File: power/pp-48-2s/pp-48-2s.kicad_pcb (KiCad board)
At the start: 4 copper layers, 150 x 80 mm, 178 parts, among them J1 BUS 40-60V, J101 NODE 1, J2 CTRL IN, J201 NODE 2, J3 CTRL OUT, J4 12V AUX OUT, J5 SWD, Q1 2N7002, Q101 BSC070N10NS5, Q102 2N7002, Q103 2N7002, Q104 2N7002, Q201 BSC070N10NS5, Q202 2N7002, Q203 2N7002, Q204 2N7002, U1 LM5164DDA, U101 LM5069MM-2, U102 INA238AIDGSR, U103 74LVC1G74, U104 TLP176AM, U105 TLP176AM, U106 TLP291, U2 LM5164DDA, U201 LM5069MM-2, U202 INA238AIDGSR, U203 74LVC1G74, U204 TLP176AM, U205 TLP176AM, U206 TLP291, U3 STM32G0B1CBT6, U4 ISO1640BD, U5 ISO7721D, U6 MCP23017-E/SO, X101 PM-19V-200W, X102 J2 AUX, X201 PM-19V-200W, X202 J2 AUX, Y1 8MHz

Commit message: power: PP-48-2S WIP checkpoint: placed, power copper, gndpour, KRT routed
tools/place.py (sockets, node connectors, bus terminal, MCU corner),
tools/power.py (VBUS trunk/artery/bar on B.Cu, slot SENSE/OUT/NODE,
GND stubs for fine-pitch pads, GND zones into the kept group),
tools/syncfields.py; gensch.py fills LCSC numbers (116 of 174).
Outline 150 x 95 mm, clearance 0.15 mm, KRT with --ordering mps
--no-stub-layer-swap. DRC: 4 unconnected (+3V3 C203, /FB2 C13,
/S1_ID U3, /S1_LQ U103), 2 clearance (S1_OUT/S1_PGD 0.149 mm),
3 starved thermals, silk untouched. Netlist pp-48-2s.xml matches
the schematic.
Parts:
- moved C25 371.0 mm to (239.0, 135.5)
- moved U3 368.3 mm to (229.0, 113.0)
- moved U4 364.7 mm to (239.0, 113.0), turned to 90 degrees
- moved R20 362.9 mm to (242.5, 150.0)
- moved C26 360.3 mm to (242.0, 135.5)
- moved JP2 359.8 mm to (237.5, 153.0)
- moved R28 358.4 mm to (236.0, 140.5)
- moved J2 352.4 mm to (245.8, 118.5), turned to 90 degrees
- moved R21 348.8 mm to (242.5, 153.0)
- moved U5 348.2 mm to (239.0, 122.0), turned to 90 degrees
- moved R29 347.5 mm to (239.0, 140.5)
- moved JP3 346.3 mm to (237.5, 156.0)
- moved C205 343.7 mm to (210.0, 166.0)
- moved C27 341.8 mm to (236.0, 138.0)
- moved U2 341.7 mm to (183.0, 108.0)
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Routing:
- net GND: track 0.00 -> 947.4 mm, vias 0 -> 261
- net +3V3: track 0.00 -> 475.4 mm, vias 0 -> 55
- net /VBUS: track 0.00 -> 310.3 mm, vias 0 -> 21
- net /SCL2: track 0.00 -> 219.7 mm, vias 0 -> 19
- net /SDA2: track 0.00 -> 205.8 mm, vias 0 -> 21
- net /S1_OFF: track 0.00 -> 177.5 mm, vias 0 -> 6
- net /S1_LED: track 0.00 -> 168.9 mm, vias 0 -> 10
- net /S2_NODE: track 0.00 -> 159.9 mm
- net /S1_LCLR: track 0.00 -> 159.4 mm, vias 0 -> 15
- net /S1_LQ: track 0.00 -> 140.1 mm, vias 0 -> 10
- net /S1_PGD: track 0.00 -> 139.4 mm, vias 0 -> 8
- net /S1_NODE: track 0.00 -> 137.8 mm
- net /VBUS_SNS: track 0.00 -> 130.2 mm, vias 0 -> 2
- net /S1_TEMP: track 0.00 -> 125.8 mm, vias 0 -> 8
- net /S1_PG: track 0.00 -> 119.0 mm, vias 0 -> 6
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- added copper zone on B.Cu, net GND
- added copper zone on F.Cu, net GND
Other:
- board size 150 x 80 mm -> 150 x 95 mm

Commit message: power: PP-48-2S opens closed by hand, DRC 0 unconnected / 0 clearance
tools/handroute/10-60: +3V3 C203.1, /FB2 C13.1 (+12V tap via moved
right of C13.2), /S1_LQ U103.5 (via between the pad rows, PWR west),
S1_PGD diagonal off the S1_OUT corner, /S1_ID to the MCU (via under the
LQFP body, PWR lane at y 133.3), +3V3 pad stubs restored after prune.
Dangling KRT leftovers pruned, GND refilled. Left: 4 starved_thermal
warnings, silk. Flow comment in pcbkit.toml, handoff updated.
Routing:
- net /S1_ID: track 54.5 -> 140.7 mm, vias 5 -> 6
- net GND: track 947.4 -> 907.5 mm
- net /S1_LQ: track 140.1 -> 147.4 mm
- net +3V3: track 475.4 -> 482.1 mm, vias 55 -> 56
- net /FB2: track 25.0 -> 28.1 mm
- net +12V: track 78.7 -> 79.8 mm

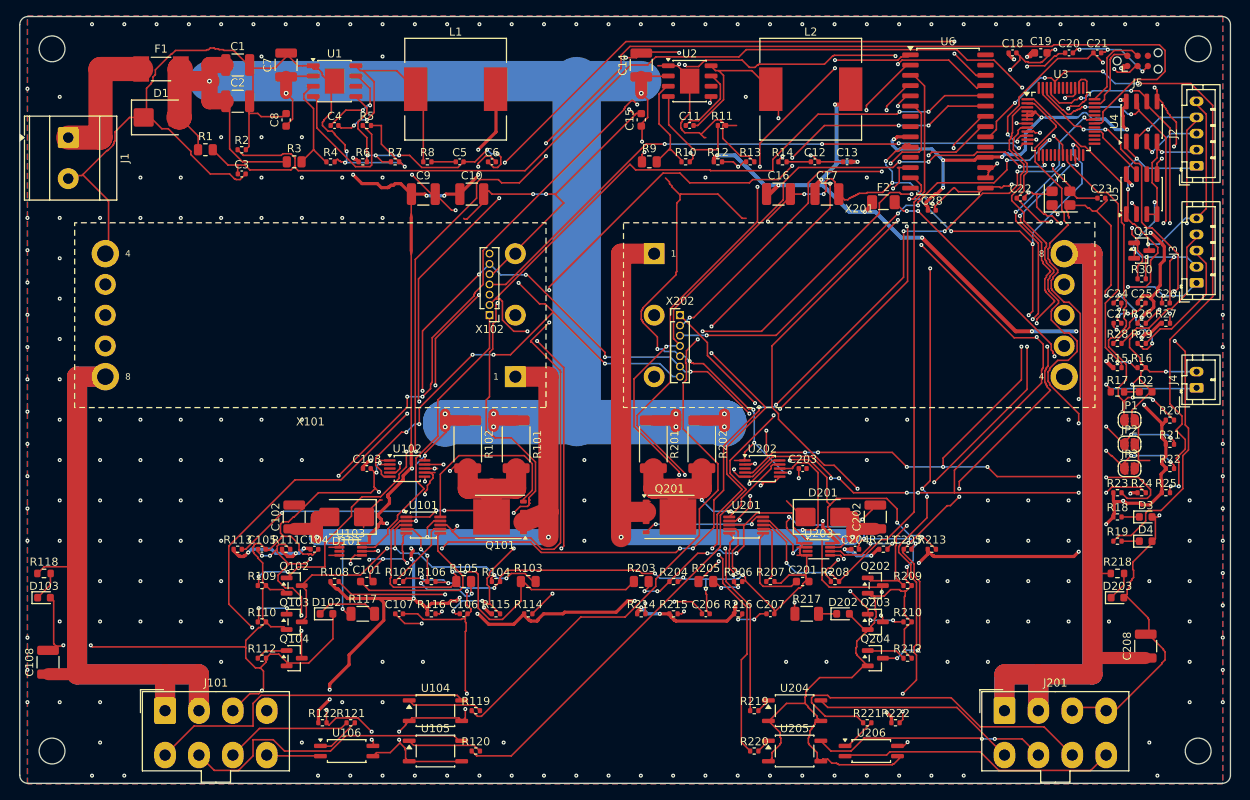
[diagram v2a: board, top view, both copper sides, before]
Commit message: power: PP-48-2S silk tidied and connector labels placed
pcbkit silk (values to Fab, small parts' refs hidden, 52 refs placed)
and connlabels (names for the 9 connectors, pin legends on J1, J4,
X102, X202; J2/J3 legends do not fit, see handoff). DRC: 0 unconnected,
0 clearance, 0 silk overlap; 4 starved_thermal and 1 silk_edge warning.
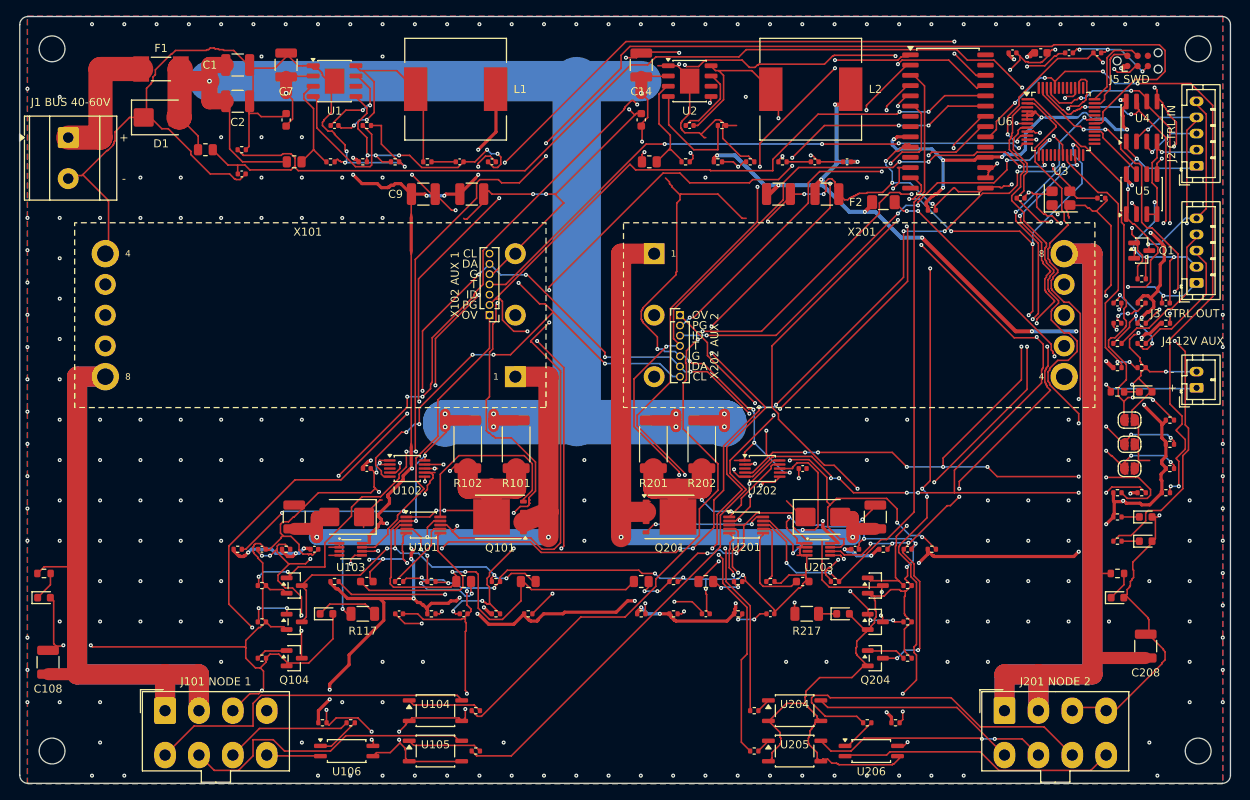
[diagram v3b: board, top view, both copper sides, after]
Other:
- board text added: "+"
- board text added: "-"
- board text added: "CL"
- board text added: "DA"
- board text added: "G"
- board text added: "ID"
- board text added: "J1 BUS 40-60V"
- board text added: "J101 NODE 1"
- board text added: "J2 CTRL IN"
- board text added: "J201 NODE 2"
- board text added: "J3 CTRL OUT"
- board text added: "J4 12V AUX"
- board text added: "J5 SWD"
- board text added: "OV"
- board text added: "PG"
- board text added: "T"
- board text added: "X102 AUX 1"
- board text added: "X202 AUX 2"

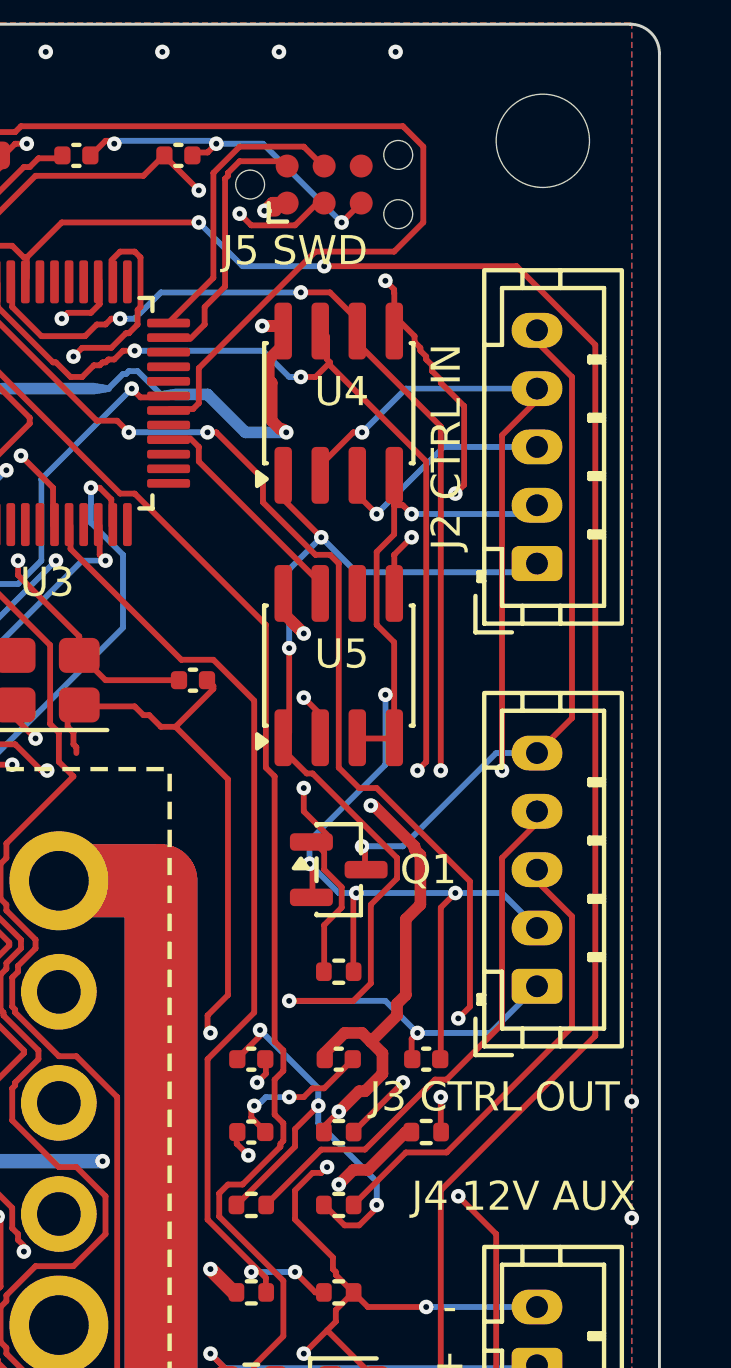
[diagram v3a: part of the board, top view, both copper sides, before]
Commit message: power: PP-48-2S J2/J3 moved 1.7 mm inboard, corridor rerouted, pin legends on all headers
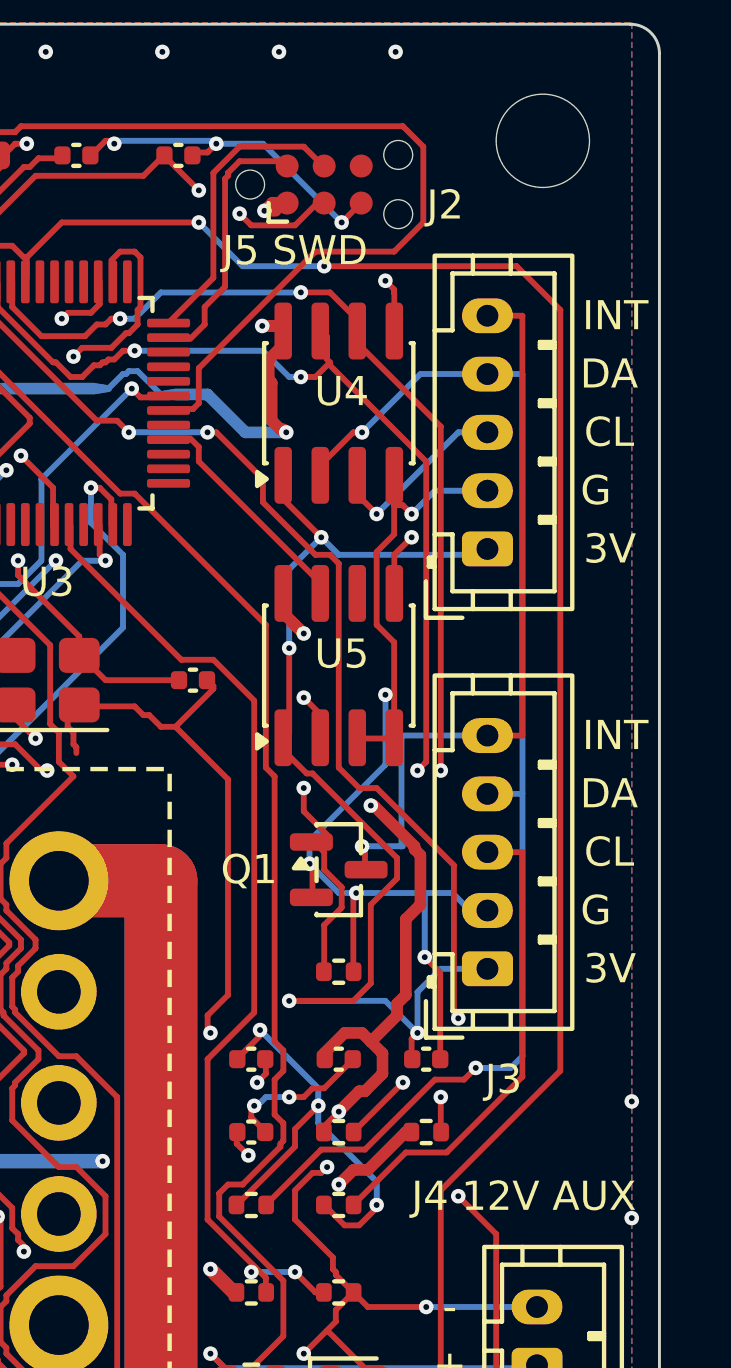
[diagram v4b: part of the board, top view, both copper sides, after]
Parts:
- moved J3 1.80 mm to (244.1, 132.4)
- moved J2 1.77 mm to (244.1, 118.0)
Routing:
- net GND: track 907.5 -> 898.2 mm, vias 261 -> 260
- net /CTRL_GND: track 49.6 -> 46.6 mm
- net /CTRL_INT: track 23.1 -> 25.6 mm
- net /CTRL_3V3: track 57.4 -> 55.2 mm
- net /CTRL_SDA: track 41.4 -> 43.7 mm
- net /CTRL_SCL: track 38.1 -> 39.3 mm
- net /EXP_IRQ: track 87.5 -> 86.5 mm
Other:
- board text added: "3V"
- board text added: "INT"
- board text added: "J2"
- board text added: "J3"
- board text removed: "J2 CTRL IN"
- board text removed: "J3 CTRL OUT"

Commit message: power: PP-48-2S schematic regenerated as drawn hierarchical sheets (ADR 0002)
tools/gensch.py now writes a root sheet and sheets/{input,bucks,mcu,link,
expanders,slot}.kicad_sch from the drawing engine in tools/sch (blocks
in tools/sch/blocks); the slot is one file instantiated per slot.
ERC 0 (--severity-all). tools/schcheck.py: every (ref, pin) -> net
identical to the previous flat netlist, 71 nets renamed to sheet-path
names, 4 expected field differences (shared slot sheet). Board relinked
with pcbkit relink: 174 paths, 71 nets, DRC unchanged (0 unconnected,
4 starved_thermal, 1 silk_edge). power.py and the handroute plans carry
the new net names. Regenerate twice is byte identical.
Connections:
- net /ADR0 renamed /MCU/ADR0
- net /ADR1 renamed /MCU/ADR1
- net /ADR2 renamed /MCU/ADR2
- net /BST1 renamed /Bucks/BST1
- net /BST2 renamed /Bucks/BST2
- net /CTRL_3V3 renamed CTRL_3V3
- net /CTRL_GND renamed CTRL_GND
- net /CTRL_INT renamed /Link/CTRL_INT
- net /CTRL_SCL renamed /Link/CTRL_SCL
- net /CTRL_SDA renamed /Link/CTRL_SDA
- net /EN1 renamed /Bucks/EN1
- net /EN2 renamed /Bucks/EN2
- net /FB1 renamed /Bucks/FB1
- net /FB2 renamed /Bucks/FB2
- net /INJ1 renamed /Bucks/INJ1
- net /INJ2 renamed /Bucks/INJ2
- net /ISO_OUTA renamed /Link/ISO_OUTA
- net /LED12_K renamed /Bucks/LED12_K
- net /LED33_K renamed /Bucks/LED33_K
- net /LEDRUN_K renamed /MCU/LEDRUN_K
- net /LED_RUN renamed /MCU/LED_RUN
- net /NRST renamed /MCU/NRST
- net /OSC_IN renamed /MCU/OSC_IN
- net /OSC_OUT renamed /MCU/OSC_OUT
- net /RON1 renamed /Bucks/RON1
- net /RON2 renamed /Bucks/RON2
- net /S1_GATE renamed /Slot 1/GATE
- net /S1_LCLR_D renamed /Slot 1/LCLR_D
- net /S1_NL_K renamed /Slot 1/NL_K
- net /S1_NODE renamed /Slot 1/NODE
- net /S1_ONL_K renamed /Slot 1/ONL_K
- net /S1_OUT renamed /Slot 1/OUT
- net /S1_OVK renamed /Slot 1/OVK
- net /S1_OVLO renamed /Slot 1/OVLO
- net /S1_PLED_A renamed /Slot 1/PLED_A
- net /S1_PLED_N renamed /Slot 1/PLED_N
- net /S1_PLED_P renamed /Slot 1/PLED_P
- net /S1_PWR renamed /Slot 1/PWR
- net /S1_PWRD_A renamed /Slot 1/PWRD_A
- net /S1_PWR_SW renamed /Slot 1/PWR_SW
- net /S1_RSTD_A renamed /Slot 1/RSTD_A
- net /S1_RST_SW renamed /Slot 1/RST_SW
- net /S1_SENSE renamed /Slot 1/SENSE
- net /S1_TIMER renamed /Slot 1/TIMER
- net /S1_UVLO renamed /Slot 1/UVLO
- net /S2_GATE renamed /Slot 2/GATE
- net /S2_LCLR_D renamed /Slot 2/LCLR_D
- net /S2_NL_K renamed /Slot 2/NL_K
- net /S2_NODE renamed /Slot 2/NODE
- net /S2_ONL_K renamed /Slot 2/ONL_K
- net /S2_OUT renamed /Slot 2/OUT
- net /S2_OVK renamed /Slot 2/OVK
- net /S2_OVLO renamed /Slot 2/OVLO
- net /S2_PLED_A renamed /Slot 2/PLED_A
- net /S2_PLED_N renamed /Slot 2/PLED_N
- net /S2_PLED_P renamed /Slot 2/PLED_P
- net /S2_PWR renamed /Slot 2/PWR
- net /S2_PWRD_A renamed /Slot 2/PWRD_A
- net /S2_PWR_SW renamed /Slot 2/PWR_SW
- net /S2_RSTD_A renamed /Slot 2/RSTD_A
- net /S2_RST_SW renamed /Slot 2/RST_SW
- net /S2_SENSE renamed /Slot 2/SENSE
- net /S2_TIMER renamed /Slot 2/TIMER
- net /S2_UVLO renamed /Slot 2/UVLO
- net /SW1 renamed /Bucks/SW1
- net /SW2 renamed /Bucks/SW2
- net /SWCLK renamed /MCU/SWCLK
- net /SWDIO renamed /MCU/SWDIO
- net /V12_OUT renamed /Bucks/V12_OUT
- net /VBUS renamed VBUS
- net /VBUS_IN renamed /Input/VBUS_IN

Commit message: power: PP-48-2S four fixes: LED polarity, LM5164 ripple network, latch clear driver, brick sense checked
LEDs: Device:LED pin 1 is K; every LED had the resistor on pin 1 and
GND on pin 2. Nets swapped (LEDnn_K -> LEDnn_A), footprints turned 180
degrees (plan 80). Ripple injection: TI SNVSAU4D Table 6-1 / Fig 7-1
have CA node -> VOUT and CB node -> FB; tables fixed, C5/C6 and
C12/C13 swapped places and rewired on the board (plans 81, 82). Latch
clear: Sn_LCLR now drives the Q104/Q204 gate (+ R112/R212); the latch
node is /Slot n/CLRN (plans 81, 83). Brick SENSE+/-: the PM-19V-200W
module leaves pins 5-7 unconnected, X1.5/X1.7 stay NC.
ERC 0; schcheck shows exactly the intended pin changes; board relinked
with pcbkit relink --allow-shorts and hand-fixed; gndpour, silk,
connlabels re-run; DRC 5 warnings as before, 0 unconnected.
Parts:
- moved C12 4.00 mm to (202.5, 118.0)
- moved C13 4.00 mm to (198.5, 118.0)
- moved C5 4.00 mm to (158.5, 118.0)
- moved C6 4.00 mm to (154.5, 118.0)
- turned D102 to 180 degrees
- turned D103 to 180 degrees
- turned D2 to 180 degrees
- turned D202 to 180 degrees
- turned D203 to 180 degrees
- turned D3 to 180 degrees
- turned D4 to 180 degrees
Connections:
- C105 pad 1: /S1_LCLR -> /Slot 1/CLRN
- C12 pad 2: /Bucks/FB2 -> +12V
- C13 pad 1: /Bucks/FB2 -> /Bucks/INJ2
- C13 pad 2: +12V -> /Bucks/FB2
- C205 pad 1: /S2_LCLR -> /Slot 2/CLRN
- C5 pad 2: /Bucks/FB1 -> +3V3
- C6 pad 1: /Bucks/FB1 -> /Bucks/INJ1
- C6 pad 2: +3V3 -> /Bucks/FB1
- D102 pad 1: /Slot 1/ONL_K -> GND
- D102 pad 2: GND -> /Slot 1/ONL_A
- D103 pad 1: /Slot 1/NL_K -> GND
- D103 pad 2: GND -> /Slot 1/NL_A
- D2 pad 1: /Bucks/LED12_K -> GND
- D2 pad 2: GND -> /Bucks/LED12_A
- D202 pad 1: /Slot 2/ONL_K -> GND
- D202 pad 2: GND -> /Slot 2/ONL_A
- D203 pad 1: /Slot 2/NL_K -> GND
- D203 pad 2: GND -> /Slot 2/NL_A
- D3 pad 1: /Bucks/LED33_K -> GND
- D3 pad 2: GND -> /Bucks/LED33_A
- D4 pad 1: /MCU/LEDRUN_K -> GND
- D4 pad 2: GND -> /MCU/LEDRUN_A
- Q104 pad 1: /Slot 1/LCLR_D -> /S1_LCLR
- Q104 pad 3: /S1_LCLR -> /Slot 1/CLRN
- Q204 pad 1: /Slot 2/LCLR_D -> /S2_LCLR
- Q204 pad 3: /S2_LCLR -> /Slot 2/CLRN
- R111 pad 2: /S1_LCLR -> /Slot 1/CLRN
- R112 pad 1: /Slot 1/LCLR_D -> /S1_LCLR
- R117 pad 2: /Slot 1/ONL_K -> /Slot 1/ONL_A
- R118 pad 2: /Slot 1/NL_K -> /Slot 1/NL_A
- R17 pad 2: /Bucks/LED12_K -> /Bucks/LED12_A
- R18 pad 2: /Bucks/LED33_K -> /Bucks/LED33_A
- R19 pad 2: /MCU/LEDRUN_K -> /MCU/LEDRUN_A
- R211 pad 2: /S2_LCLR -> /Slot 2/CLRN
- R212 pad 1: /Slot 2/LCLR_D -> /S2_LCLR
- R217 pad 2: /Slot 2/ONL_K -> /Slot 2/ONL_A
- R218 pad 2: /Slot 2/NL_K -> /Slot 2/NL_A
- U103 pad 6: /S1_LCLR -> /Slot 1/CLRN
- U203 pad 6: /S2_LCLR -> /Slot 2/CLRN
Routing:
- net /Slot 1/CLRN: track 0.00 -> 35.4 mm, vias 0 -> 6
- net /Slot 2/CLRN: track 0.00 -> 30.4 mm, vias 0 -> 5
- net /S1_LCLR: track 159.4 -> 149.6 mm, vias 15 -> 10
- net /S2_LCLR: track 96.8 -> 87.9 mm, vias 9 -> 4
- net /Bucks/FB1: track 33.2 -> 24.6 mm, vias 5 -> 3
- net /Slot 1/ONL_K: track 7.79 -> 0.00 mm
- net /Slot 1/ONL_A: track 0.00 -> 7.79 mm
- net /Bucks/INJ2: track 3.02 -> 10.6 mm
- net /Bucks/INJ1: track 3.02 -> 8.42 mm
- net /Slot 2/LCLR_D: track 4.77 -> 0.00 mm
- net /Slot 1/LCLR_D: track 3.97 -> 0.00 mm
- net /Slot 2/NL_K: track 3.66 -> 0.00 mm
- net /Slot 2/NL_A: track 0.00 -> 3.66 mm
- net /Slot 1/NL_K: track 3.66 -> 0.00 mm
- net /Slot 1/NL_A: track 0.00 -> 3.66 mm
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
